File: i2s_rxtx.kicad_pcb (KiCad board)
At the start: 2 copper layers, 90.9 x 53.3 mm, 21 parts, among them IC1 AM26C32, IC2 AM26C31, IC3 AM26C31, J1 CONN_01x02, J2 RJ45_Shielded, J3 CONN_01x05, J4 RJ45_Shielded, J5 RJ45_Shielded

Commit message: --update
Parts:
- added R5: 500K, Resistor_SMD:R_0805_2012Metric_Pad1.15x1.40mm_HandSolder, F.Cu at (85.9, 75.8)
- added R6: 500K, Resistor_SMD:R_0805_2012Metric_Pad1.15x1.40mm_HandSolder, F.Cu at (94.0, 80.6)
- added R7: 500K, Resistor_SMD:R_0805_2012Metric_Pad1.15x1.40mm_HandSolder, F.Cu at (97.8, 68.3)
- added R8: 500K, Resistor_SMD:R_0805_2012Metric_Pad1.15x1.40mm_HandSolder, F.Cu at (93.1, 74.4)
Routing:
- net GND: track 47.7 -> 59.5 mm, vias 13 -> 16
- net I2S_CH34: track 68.9 -> 70.4 mm

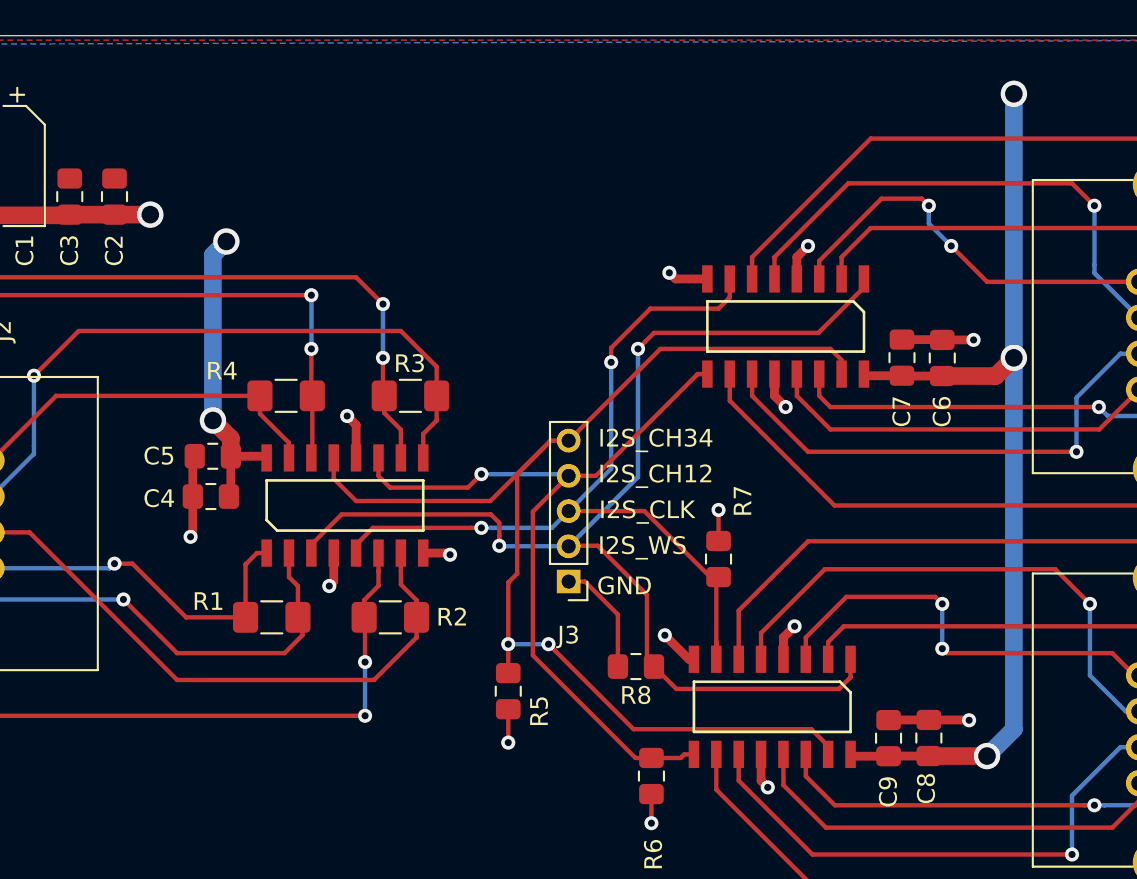
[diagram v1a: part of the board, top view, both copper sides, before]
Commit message: -- changed vias
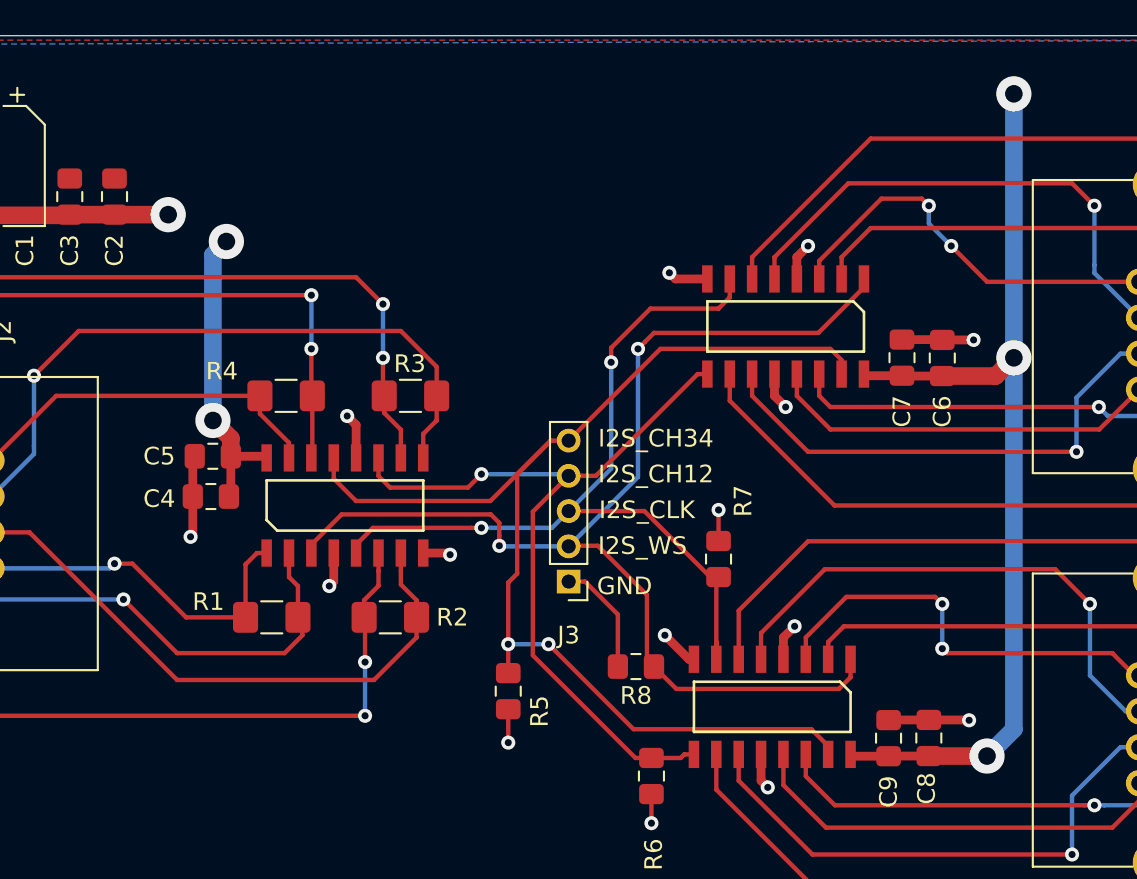
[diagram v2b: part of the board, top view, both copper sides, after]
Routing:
- net GND: track 59.5 -> 60.5 mm
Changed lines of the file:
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@@
     (via_min_drill 0.3)
     (user_via 0.7 0.3)
-    (user_via 1.5 1)
+    (user_via 2 1)
     (user_via 2 1.5)
     (user_via 2.5 2)
@@
   (segment (start 106.139 57.912) (end 106.045 57.818) (width 0.5) (layer F.Cu) (net 1))
   (segment (start 108.204 57.912) (end 106.139 57.912) (width 0.5) (layer F.Cu) (net 1))
-  (via (at 114.554 56.896) (size 1.5) (drill 1) (layers F.Cu B.Cu) (net 1))
+  (via (at 114.554 56.896) (size 2) (drill 1) (layers F.Cu B.Cu) (net 1))
   (segment (start 110.49 57.93) (end 113.52 57.93) (width 1) (layer F.Cu) (net 1))
   (segment (start 113.52 57.93) (end 114.554 56.896) (width 1) (layer F.Cu) (net 1))
-  (via (at 113.03 79.502) (size 1.5) (drill 1) (layers F.Cu B.Cu) (net 1))
+  (via (at 113.03 79.502) (size 2) (drill 1) (layers F.Cu B.Cu) (net 1))
   (segment (start 114.554 56.896) (end 114.554 77.978) (width 1) (layer B.Cu) (net 1))
   (segment (start 114.554 77.978) (end 113.03 79.502) (width 1) (layer B.Cu) (net 1))
   (segment (start 113.03 79.502) (end 109.728 79.502) (width 1) (layer F.Cu) (net 1))
-  (via (at 114.554 41.91) (size 1.5) (drill 1) (layers F.Cu B.Cu) (net 1))
+  (via (at 114.554 41.91) (size 2) (drill 1) (layers F.Cu B.Cu) (net 1))
   (segment (start 114.554 56.896) (end 114.554 41.91) (width 1) (layer B.Cu) (net 1))
-  (via (at 69.088 60.452) (size 1.5) (drill 1) (layers F.Cu B.Cu) (net 1))
+  (via (at 69.088 60.452) (size 2) (drill 1) (layers F.Cu B.Cu) (net 1))
   (segment (start 70.104 62.484) (end 70.104 61.468) (width 1) (layer F.Cu) (net 1))
   (segment (start 70.104 61.468) (end 69.088 60.452) (width 1) (layer F.Cu) (net 1))
-  (via (at 69.85 50.292) (size 1.5) (drill 1) (layers F.Cu B.Cu) (net 1))
+  (via (at 69.85 50.292) (size 2) (drill 1) (layers F.Cu B.Cu) (net 1))
   (segment (start 69.088 60.452) (end 69.088 51.054) (width 1) (layer B.Cu) (net 1))
   (segment (start 69.088 51.054) (end 69.85 50.292) (width 1) (layer B.Cu) (net 1))
@@
   (segment (start 56.134 48.807) (end 60.921 48.807) (width 1) (layer F.Cu) (net 2))
   (segment (start 60.96 48.768) (end 63.5 48.768) (width 1) (layer F.Cu) (net 2))
-  (via (at 65.532 48.768) (size 1.5) (drill 1) (layers F.Cu B.Cu) (net 2))
-  (segment (start 63.5 48.768) (end 65.532 48.768) (width 1) (layer F.Cu) (net 2))
   (segment (start 51.125 48.807) (end 50.546 48.228) (width 1) (layer F.Cu) (net 2))
   (segment (start 56.134 48.807) (end 51.125 48.807) (width 1) (layer F.Cu) (net 2))
@@
   (segment (start 92.075 71.465) (end 90.206 69.596) (width 0.25) (layer F.Cu) (net 2))
   (segment (start 92.075 74.422) (end 92.075 71.465) (width 0.25) (layer F.Cu) (net 2))
+  (via (at 66.548 48.768) (size 2) (drill 1) (layers F.Cu B.Cu) (net 2))
+  (segment (start 63.5 48.768) (end 66.548 48.768) (width 1) (layer F.Cu) (net 2))
   (segment (start 60.186 59.055) (end 71.755 59.055) (width 0.25) (layer F.Cu) (net 3))
   (segment (start 56.517 62.724) (end 60.186 59.055) (width 0.25) (layer F.Cu) (net 3))

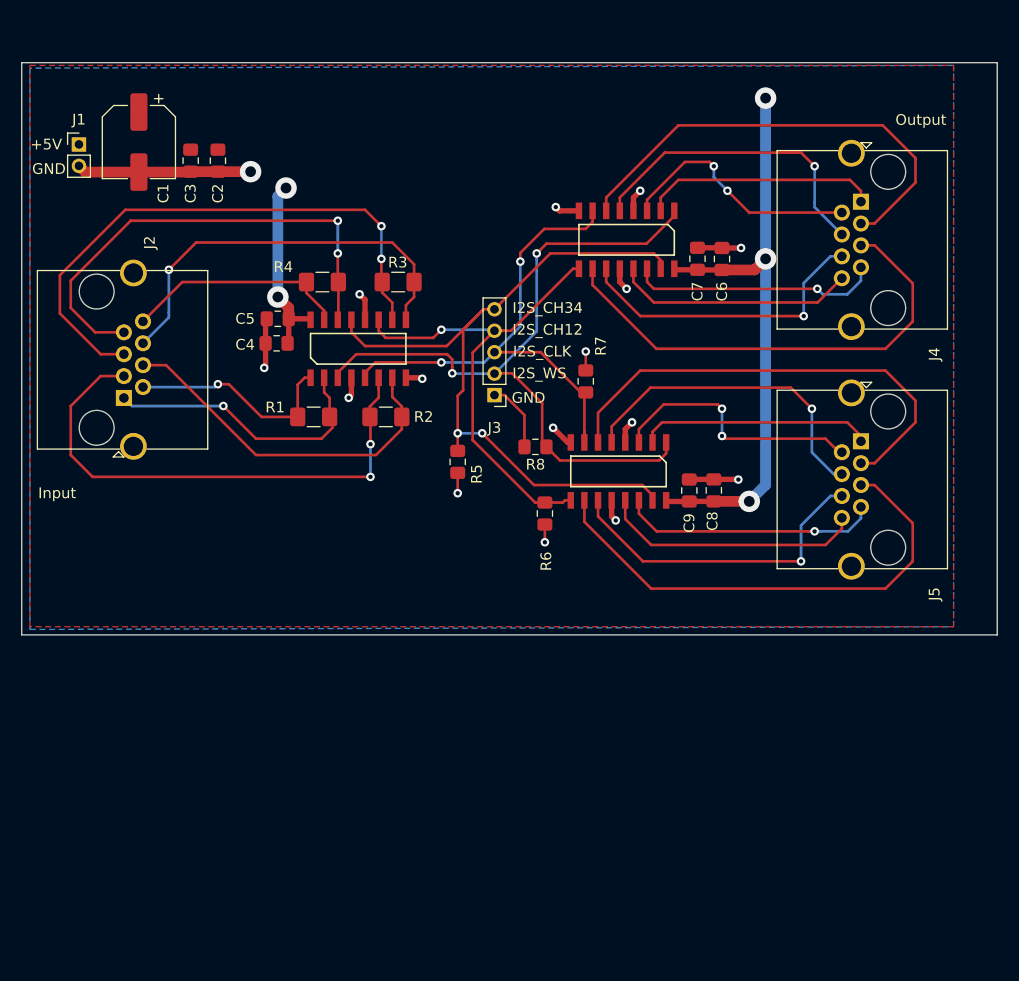
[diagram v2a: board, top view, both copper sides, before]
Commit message: -- added mounting holes
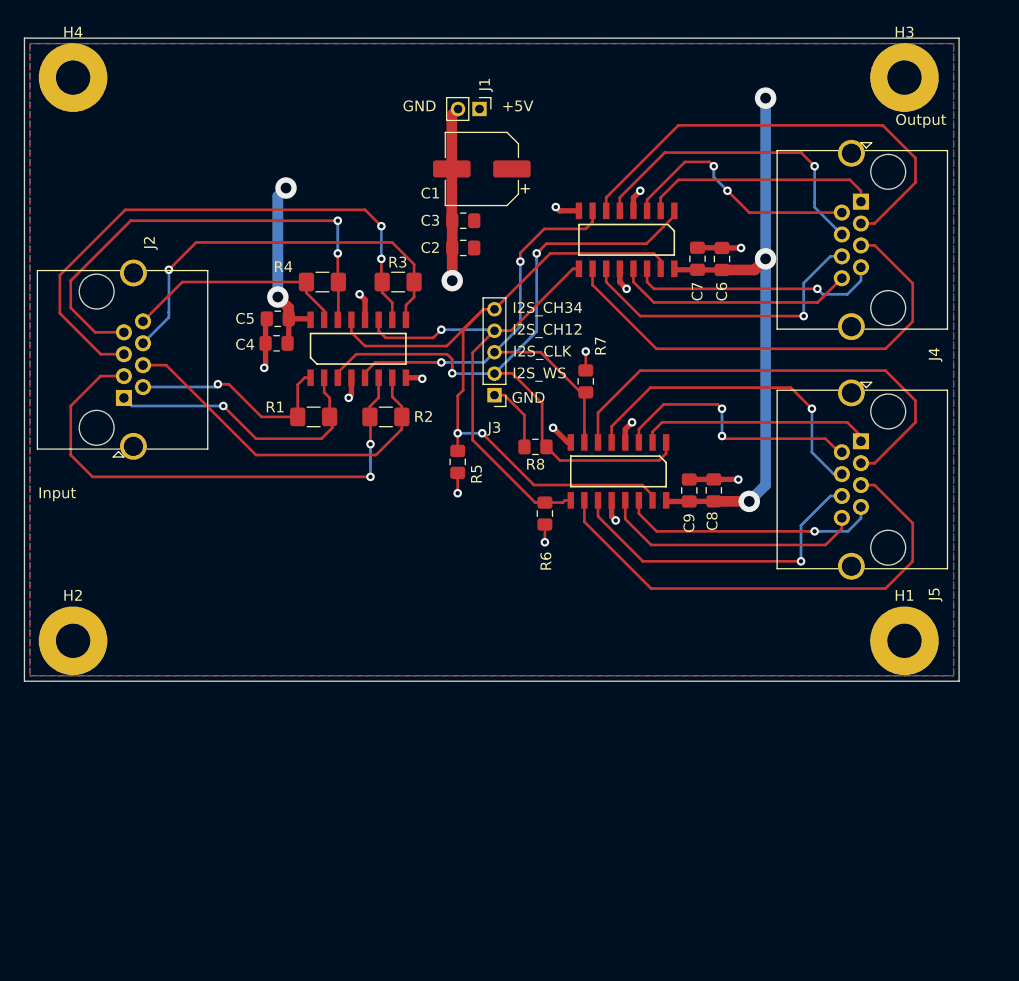
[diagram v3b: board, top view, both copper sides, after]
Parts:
- added H1: MountingHole, MountingHole:MountingHole_3.2mm_M3_Pad, F.Cu at (127.5, 92.5)
- added H2: MountingHole, MountingHole:MountingHole_3.2mm_M3_Pad, F.Cu at (50.0, 92.5)
- added H3: MountingHole, MountingHole:MountingHole_3.2mm_M3_Pad, F.Cu at (127.5, 40.0)
- added H4: MountingHole, MountingHole:MountingHole_3.2mm_M3_Pad, F.Cu at (50.0, 40.0)
- moved J1 37.5 mm to (87.9, 42.9), turned to 270 degrees
- moved C1 32.1 mm to (88.1, 48.5), turned to 180 degrees
- moved C3 26.0 mm to (86.4, 53.3), turned to 180 degrees
- moved C2 24.3 mm to (86.4, 55.9), turned to 180 degrees
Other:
- board size 90.9 x 53.3 mm -> 87.1 x 59.9 mm

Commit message: adjusted pcb layout to new termination network
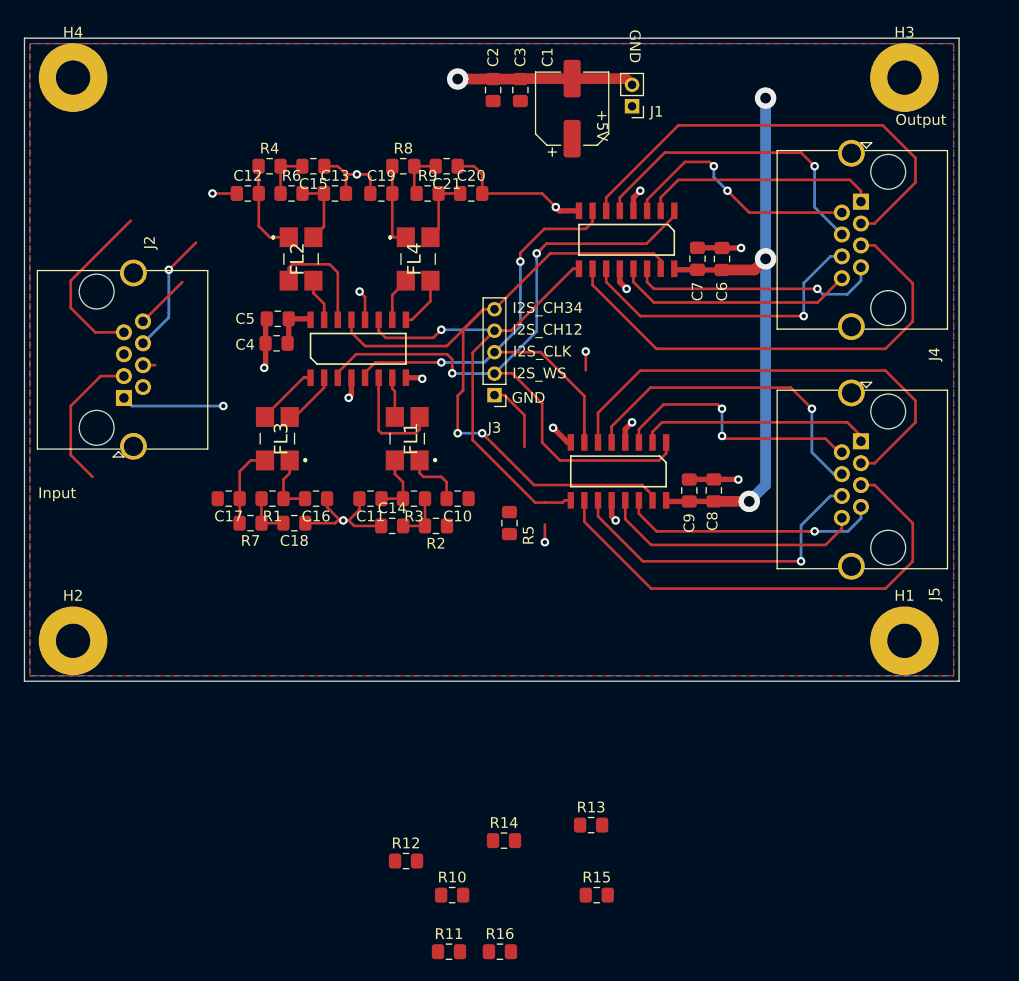
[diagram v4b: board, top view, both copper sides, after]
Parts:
- added C10: C, Capacitor_SMD:C_0805_2012Metric_Pad1.15x1.40mm_HandSolder, F.Cu at (85.8, 79.2)
- added C11: C, Capacitor_SMD:C_0805_2012Metric_Pad1.15x1.40mm_HandSolder, F.Cu at (77.7, 79.2)
- added C12: C, Capacitor_SMD:C_0805_2012Metric_Pad1.15x1.40mm_HandSolder, F.Cu at (66.3, 50.8)
- added C13: C, Capacitor_SMD:C_0805_2012Metric_Pad1.15x1.40mm_HandSolder, F.Cu at (74.4, 50.8)
- added C14: 4.7nF, Capacitor_SMD:C_0805_2012Metric_Pad1.15x1.40mm_HandSolder, F.Cu at (79.7, 81.8)
- added C15: 4.7nF, Capacitor_SMD:C_0805_2012Metric_Pad1.15x1.40mm_HandSolder, F.Cu at (72.4, 48.3)
- added C16: C, Capacitor_SMD:C_0805_2012Metric_Pad1.15x1.40mm_HandSolder, F.Cu at (72.7, 79.2)
- added C17: C, Capacitor_SMD:C_0805_2012Metric_Pad1.15x1.40mm_HandSolder, F.Cu at (64.5, 79.2)
- added C18: 4.7nF, Capacitor_SMD:C_0805_2012Metric_Pad1.15x1.40mm_HandSolder, F.Cu at (70.6, 81.5)
- added C19: C, Capacitor_SMD:C_0805_2012Metric_Pad1.15x1.40mm_HandSolder, F.Cu at (78.7, 50.8)
- added C20: C, Capacitor_SMD:C_0805_2012Metric_Pad1.15x1.40mm_HandSolder, F.Cu at (87.1, 50.8)
- added C21: 4.7nF, Capacitor_SMD:C_0805_2012Metric_Pad1.15x1.40mm_HandSolder, F.Cu at (84.8, 48.3)
- added FL1: EMI_Filter_CommonMode, agg:B82789_PinSwap, F.Cu at (81.4, 73.7)
- added FL2: EMI_Filter_CommonMode, agg:B82789_PinSwap, F.Cu at (71.0, 56.9)
- added FL3: EMI_Filter_CommonMode, agg:B82789_PinSwap, F.Cu at (69.3, 73.7)
- added FL4: EMI_Filter_CommonMode, agg:B82789_PinSwap, F.Cu at (81.9, 56.9)
- added R10: 2K2, Resistor_SMD:R_0805_2012Metric_Pad1.15x1.40mm_HandSolder, F.Cu at (85.3, 116.2)
- added R11: 3K9, Resistor_SMD:R_0805_2012Metric_Pad1.15x1.40mm_HandSolder, F.Cu at (85.0, 121.5)
- added R12: 2K2, Resistor_SMD:R_0805_2012Metric_Pad1.15x1.40mm_HandSolder, F.Cu at (81.0, 113.0)
- added R13: 3K9, Resistor_SMD:R_0805_2012Metric_Pad1.15x1.40mm_HandSolder, F.Cu at (98.3, 109.7)
- added R14: 2K2, Resistor_SMD:R_0805_2012Metric_Pad1.15x1.40mm_HandSolder, F.Cu at (90.2, 111.1)
- added R15: 3K9, Resistor_SMD:R_0805_2012Metric_Pad1.15x1.40mm_HandSolder, F.Cu at (98.8, 116.2)
- added R16: 3K9, Resistor_SMD:R_0805_2012Metric_Pad1.15x1.40mm_HandSolder, F.Cu at (89.8, 121.5)
- added R9: 50R, Resistor_SMD:R_0805_2012Metric_Pad1.15x1.40mm_HandSolder, F.Cu at (83.0, 50.8)
- R1, R2, R3, R4: value 100R -> 50R; footprint Resistor_SMD:R_1206_3216Metric_Pad1.42x1.75mm_HandSolder -> Resistor_SMD:R_0805_2012Metric_Pad1.15x1.40mm_HandSolder
- R5: value 500K -> 2K2
- R6, R7, R8: value 500K -> 50R
- moved R6 38.1 mm to (70.4, 50.8), turned to 0 degrees
- moved R7 33.9 mm to (66.5, 81.5), turned to 180 degrees
- moved R8 28.9 mm to (80.8, 48.3), turned to 0 degrees
- moved R3 20.2 mm to (81.8, 79.2), turned to 180 degrees
- moved C2 15.0 mm to (89.2, 41.2), turned to 90 degrees
- moved J1 14.2 mm to (102.1, 42.7), turned to 180 degrees
- moved C3 13.3 mm to (91.7, 41.2), turned to 90 degrees
- moved R4 11.9 mm to (68.3, 48.3), turned to 0 degrees
- moved R2 11.2 mm to (83.8, 81.8), turned to 180 degrees
- moved C1 10.1 mm to (96.5, 42.9), turned to 90 degrees
- moved R1 8.53 mm to (68.6, 79.2)
- moved R5 7.47 mm to (90.7, 81.5)
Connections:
- IC1 pad 1: WS_Z -> Net-(FL3-Pad4)
- IC1 pad 10: CH_12_Y -> Net-(FL4-Pad2)
- IC1 pad 14: CH_34_Y -> Net-(FL2-Pad2)
- IC1 pad 15: CH_34_Z -> Net-(FL2-Pad4)
- IC1 pad 2: WS_Y -> Net-(FL3-Pad2)
- IC1 pad 6: CLK_Y -> Net-(FL1-Pad2)
- IC1 pad 7: CLK_Z -> Net-(FL1-Pad4)
- IC1 pad 9: CH_12_Z -> Net-(FL4-Pad4)
- J3 pad 2: I2S_WS -> I2S_WS_3V3
- J3 pad 3: I2S_CLK -> I2S_CLK_3V3
- J3 pad 4: I2S_CH12 -> I2S_CH12_3V3
- J3 pad 5: I2S_CH34 -> I2S_CH34_3V3
- R1 pad 2: WS_Z -> Net-(C18-Pad2)
- R2 pad 2: CLK_Z -> Net-(C14-Pad2)
- R3 pad 1: CH_12_Y -> Net-(C14-Pad2)
- R3 pad 2: CH_12_Z -> CLK_Z
- R4 pad 2: CH_34_Z -> Net-(C15-Pad2)
- R5 pad 1: I2S_CH34 -> I2S_WS
- R5 pad 2: GND -> I2S_WS_3V3
- R6 pad 1: I2S_CH12 -> Net-(C15-Pad2)
- R6 pad 2: GND -> CH_34_Z
- R7 pad 1: I2S_CLK -> Net-(C18-Pad2)
- R7 pad 2: GND -> WS_Z
- R8 pad 1: I2S_WS -> CH_12_Y
- R8 pad 2: GND -> Net-(C21-Pad2)
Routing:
- net CH_12_Y: track 53.4 -> 7.78 mm, vias 2 -> 0
- net GND: track 60.5 -> 93.3 mm, vias 16 -> 18
- net CLK_Y: track 49.1 -> 19.1 mm, vias 2 -> 0
- net CLK_Z: track 33.8 -> 7.03 mm
- net CH_12_Z: track 38.1 -> 17.9 mm
- net CH_34_Y: track 44.9 -> 25.2 mm, vias 2 -> 0
- net +5V: track 72.3 -> 59.4 mm, vias 5 -> 3
- net WS_Z: track 20.3 -> 7.62 mm, vias 1 -> 0
- net WS_Y: track 26.4 -> 15.4 mm
- net Net-(FL2-Pad2): track 0.00 -> 10.7 mm
- net Net-(FL1-Pad2): track 0.00 -> 10.2 mm
- net CH_34_Z: track 21.0 -> 11.7 mm
- net Net-(FL3-Pad4): track 0.00 -> 5.94 mm
- net Net-(FL3-Pad2): track 0.00 -> 5.27 mm
- net Net-(C15-Pad2): track 0.00 -> 5.09 mm
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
